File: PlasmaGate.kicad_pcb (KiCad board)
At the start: 4 copper layers, 91.5 x 52.1 mm, 161 parts, among them J101 Conn_02x08_Odd_Even, J102 Conn_02x16_Odd_Even, J103 Conn_02x20_Odd_Even, J1201 DX07S016JA1R1500, J201 HDMI_A, J202 Micro_SD_Card_Det_Hirose_DM3AT, J203 DX07S016JA1R1500, SW1201 SW_Push, SW201 SW_Push, U10 IS25LP128F-JBLE, U1001 INA236, U1002 USB3300-EZK, U1101 MT48LC16M16A2P, U1201 RP2040, U1203 W25Q16JVSS, U202 USB6B1, U203 LFE5U-85F-6BG381x, U401 NCP718xSN250, U501 INA236, U601 TLV62568DDC, U701 TLV62568DDC, U801 INA236, U901 INA236, X1 ECS-2520MV-xxx-xx, Y1001 Crystal_GND24_Small, Y201 12MHz

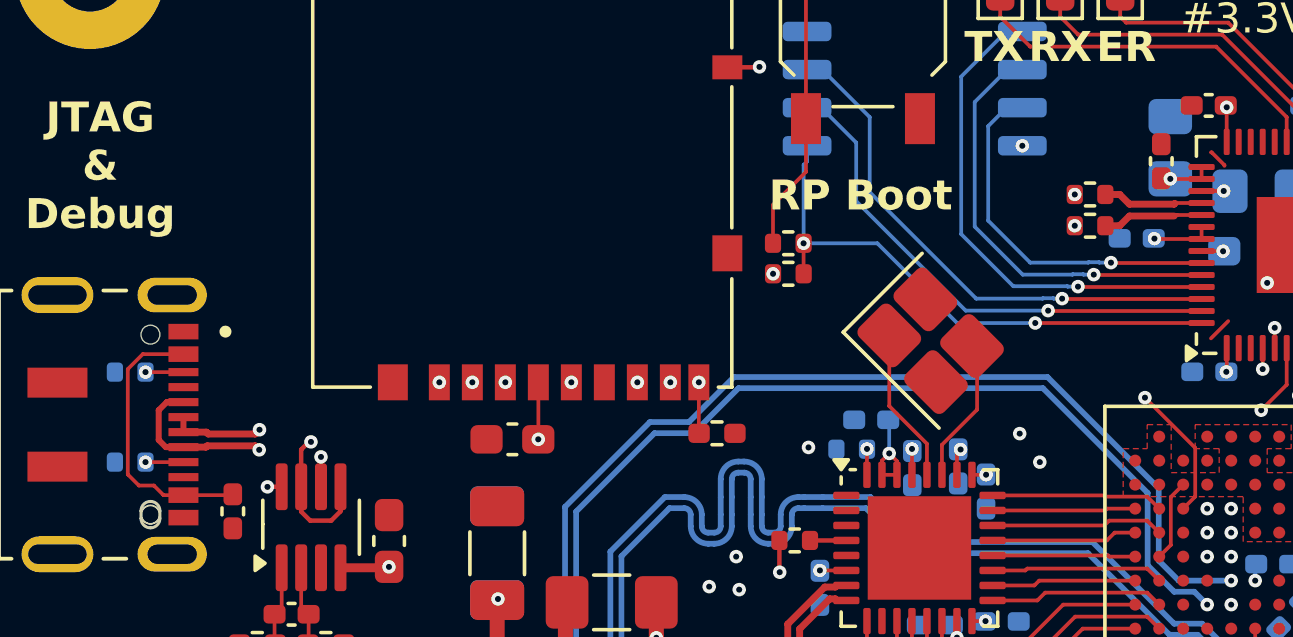
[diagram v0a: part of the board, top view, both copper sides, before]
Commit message: Fix mistakes in V1.0
Signed-off-by: Alexis Jeandet <alexis.jeandet@member.fsf.org>
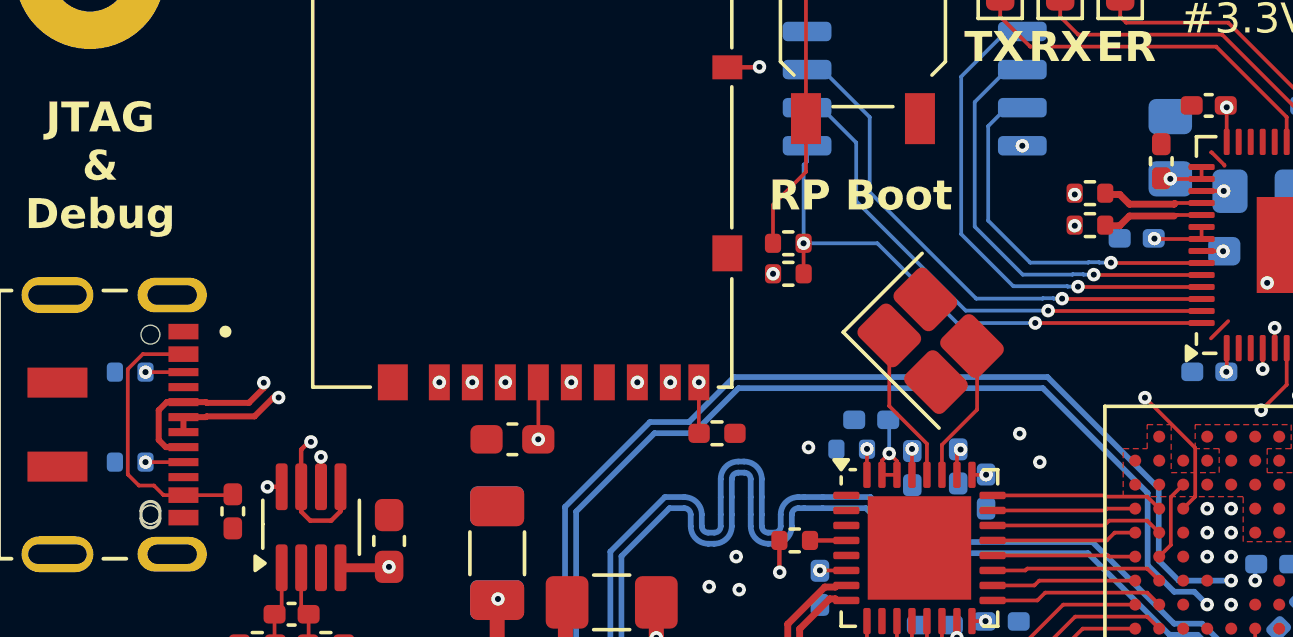
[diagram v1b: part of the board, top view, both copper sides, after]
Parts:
- R1001, R501, R801, R901: value R -> 0.1
- R1207: value 1k -> 10k
- moved R1205 1.08 mm to (103.0, 60.5)
- moved R1204 1.02 mm to (103.0, 61.5)
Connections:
- U1201 pad 46: /JTAG/USB_D+ -> /JTAG/USB_D-
- U1201 pad 47: /JTAG/USB_D- -> /JTAG/USB_D+

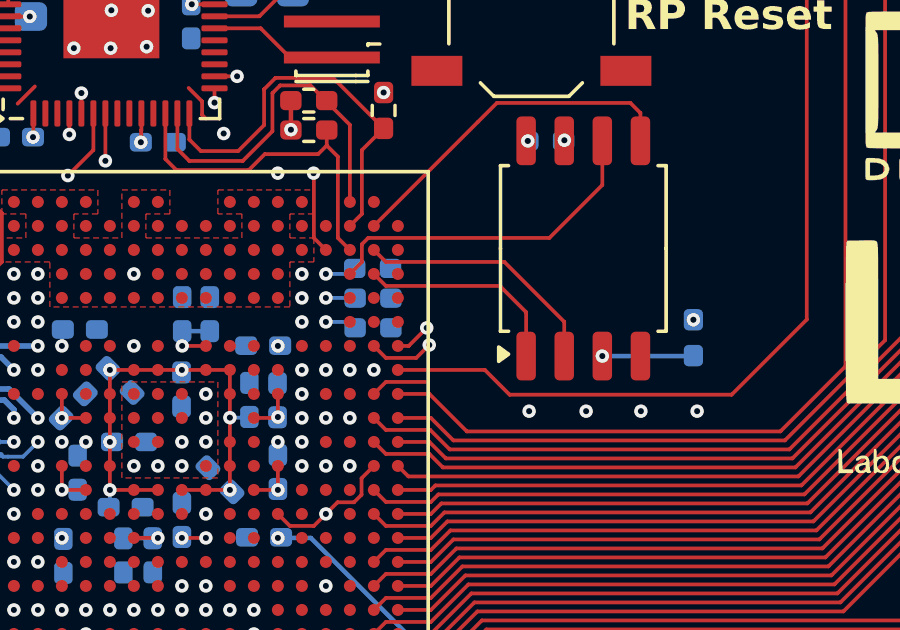
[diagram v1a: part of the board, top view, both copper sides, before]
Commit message: Fix FPGA flash connection
Signed-off-by: Alexis Jeandet <alexis.jeandet@member.fsf.org>
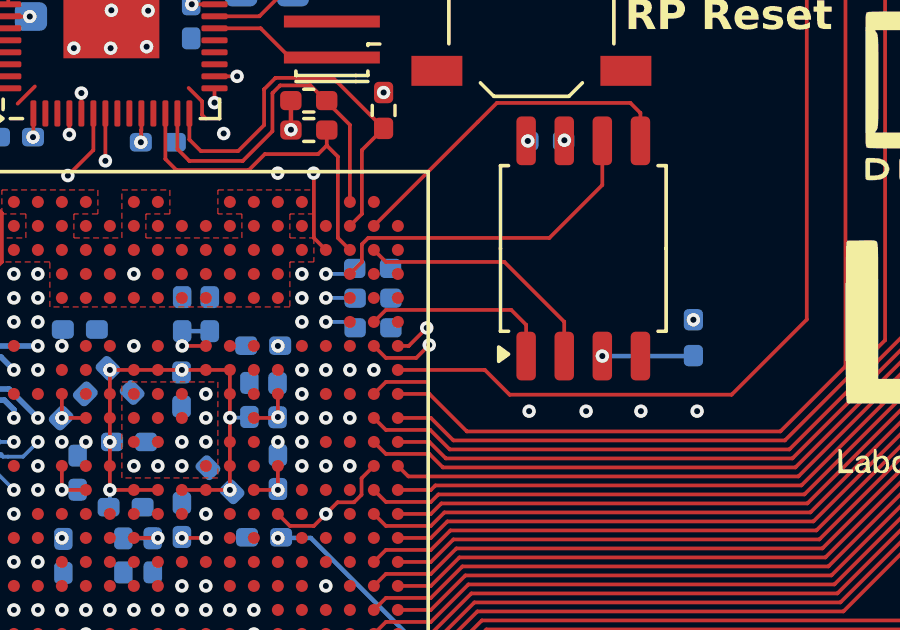
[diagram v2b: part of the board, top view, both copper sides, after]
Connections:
- U203 pad R2: unconnected-(U203H-PB15A-PadR2) -> /FPGA/FLASH_nCS
- U203 pad U2: /FPGA/FLASH_nCS -> unconnected-(U203H-PB13B-PadU2)
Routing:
- net /FPGA/FLASH_nCS: track 7.07 -> 6.49 mm
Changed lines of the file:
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@@
 	(net 110 "unconnected-(U203G-PL44A-PadG3)")
 	(net 111 "unconnected-(U203G-PL20D-PadF5)")
-	(net 112 "unconnected-(U203H-PB15A-PadR2)")
+	(net 112 "unconnected-(U203H-PB13B-PadU2)")
 	(net 113 "unconnected-(U203C-PT69A-PadD11)")
 	(net 114 "unconnected-(U203E-PR50D-PadM18)")
@@
 			(property pad_prop_bga)
 			(layers "F.Cu" "F.Mask" "F.Paste")
-			(net 112 "unconnected-(U203H-PB15A-PadR2)")
+			(net 166 "/FPGA/FLASH_nCS")
 			(pinfunction "PB15A")
 			(pintype "bidirectional")
@@
 			(property pad_prop_bga)
 			(layers "F.Cu" "F.Mask" "F.Paste")
-			(net 166 "/FPGA/FLASH_nCS")
+			(net 112 "unconnected-(U203H-PB13B-PadU2)")
 			(pinfunction "PB13B")
 			(pintype "bidirectional")
@@
 	)
 	(segment
-		(start 123.975 73.7375)
-		(end 123.975 72.275)
+		(start 123.48 72.2)
+		(end 123.975 72.695)
 		(width 0.125)
 		(layer "F.Cu")
@@
 	)
 	(segment
-		(start 123.1 71.4)
-		(end 119.300001 71.4)
+		(start 118.900002 72.6)
+		(end 119.300002 72.2)
 		(width 0.125)
 		(layer "F.Cu")
@@
 	)
 	(segment
-		(start 119.300001 71.4)
-		(end 118.900001 71)
+		(start 123.975 72.695)
+		(end 123.975 73.7375)
 		(width 0.125)
 		(layer "F.Cu")
@@
 	)
 	(segment
-		(start 123.975 72.275)
-		(end 123.1 71.4)
+		(start 119.300002 72.2)
+		(end 123.48 72.2)
 		(width 0.125)
 		(layer "F.Cu")
